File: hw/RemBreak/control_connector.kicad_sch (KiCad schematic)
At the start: 1 part, among them J5 Conn_02x06_Odd_Even

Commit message: routing in progress
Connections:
- net +3V3: now also J5.6 (Pin_6); no longer J5.3 (Pin_3)
- net +5V: now also J5.5 (Pin_5); no longer J5.4 (Pin_4)
- net ON/OFF: now also J5.3 (Pin_3); no longer J5.5 (Pin_5)
- net VBATT: now also J5.4 (Pin_4); no longer J5.6 (Pin_6)
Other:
- moved on the sheet: J5
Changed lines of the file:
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@@
 	(wire
 		(pts
-			(xy 137.16 72.39) (xy 152.4 72.39)
+			(xy 163.83 93.98) (xy 179.07 93.98)
 		)
 		(stroke
@@
 	(wire
 		(pts
-			(xy 137.16 77.47) (xy 152.4 77.47)
+			(xy 163.83 96.52) (xy 179.07 96.52)
 		)
 		(stroke
@@
 	(wire
 		(pts
-			(xy 139.7 66.04) (xy 139.7 74.93)
-		)
-		(stroke
-			(width 0)
-			(type default)
-		)
-	)
-	(wire
-		(pts
-			(xy 121.92 66.04) (xy 121.92 74.93)
-		)
-		(stroke
-			(width 0)
-			(type default)
-		)
-	)
-	(wire
-		(pts
-			(xy 109.22 85.09) (xy 124.46 85.09)
-		)
-		(stroke
-			(width 0)
-			(type default)
-		)
-	)
-	(wire
-		(pts
-			(xy 109.22 77.47) (xy 124.46 77.47)
-		)
-		(stroke
-			(width 0)
-			(type default)
-		)
-	)
-	(wire
-		(pts
-			(xy 121.92 74.93) (xy 124.46 74.93)
-		)
-		(stroke
-			(width 0)
-			(type default)
-		)
-	)
-	(wire
-		(pts
-			(xy 137.16 82.55) (xy 152.4 82.55)
+			(xy 148.59 87.63) (xy 148.59 99.06)
+		)
+		(stroke
+			(width 0)
+			(type default)
+		)
+	)
+	(wire
+		(pts
+			(xy 135.89 106.68) (xy 151.13 106.68)
+		)
+		(stroke
+			(width 0)
+			(type default)
+		)
+	)
+	(wire
+		(pts
+			(xy 135.89 96.52) (xy 151.13 96.52)
+		)
+		(stroke
+			(width 0)
+			(type default)
+		)
+	)
+	(wire
+		(pts
+			(xy 163.83 104.14) (xy 179.07 104.14)
 		)
 		(stroke
@@
 	(wire
 		(pts
-			(xy 139.7 74.93) (xy 137.16 74.93)
-		)
-		(stroke
-			(width 0)
-			(type default)
-		)
-	)
-	(wire
-		(pts
 			(xy 41.91 104.14) (xy 41.91 107.95)
 		)
@@
 	(wire
 		(pts
-			(xy 137.16 80.01) (xy 152.4 80.01)
-		)
-		(stroke
-			(width 0)
-			(type default)
-		)
-	)
-	(wire
-		(pts
-			(xy 109.22 80.01) (xy 124.46 80.01)
-		)
-		(stroke
-			(width 0)
-			(type default)
-		)
-	)
-	(wire
-		(pts
-			(xy 109.22 72.39) (xy 124.46 72.39)
-		)
-		(stroke
-			(width 0)
-			(type default)
-		)
-	)
-	(wire
-		(pts
-			(xy 109.22 82.55) (xy 124.46 82.55)
+			(xy 163.83 101.6) (xy 179.07 101.6)
+		)
+		(stroke
+			(width 0)
+			(type default)
+		)
+	)
+	(wire
+		(pts
+			(xy 135.89 101.6) (xy 151.13 101.6)
+		)
+		(stroke
+			(width 0)
+			(type default)
+		)
+	)
+	(wire
+		(pts
+			(xy 135.89 93.98) (xy 151.13 93.98)
+		)
+		(stroke
+			(width 0)
+			(type default)
+		)
+	)
+	(wire
+		(pts
+			(xy 135.89 104.14) (xy 151.13 104.14)
+		)
+		(stroke
+			(width 0)
+			(type default)
+		)
+	)
+	(wire
+		(pts
+			(xy 166.37 99.06) (xy 163.83 99.06)
+		)
+		(stroke
+			(width 0)
+			(type default)
+		)
+	)
+	(wire
+		(pts
+			(xy 148.59 99.06) (xy 151.13 99.06)
+		)
+		(stroke
+			(width 0)
+			(type default)
+		)
+	)
+	(wire
+		(pts
+			(xy 166.37 87.63) (xy 166.37 99.06)
 		)
 		(stroke
@@
 	(wire
 		(pts
-			(xy 137.16 85.09) (xy 139.7 85.09)
+			(xy 163.83 106.68) (xy 166.37 106.68)
 		)
 		(stroke
@@
 	)
 	(label "VBATT"
-		(at 152.4 77.47 180)
+		(at 179.07 96.52 180)
 		(fields_autoplaced yes)
 		(effects
@@
 	)
 	(label "LED BLUE"
-		(at 152.4 80.01 180)
+		(at 179.07 101.6 180)
 		(fields_autoplaced yes)
 		(effects
@@
 	)
 	(label "ONOFF"
-		(at 109.22 77.47 0)
+		(at 135.89 96.52 0)
 		(fields_autoplaced yes)
 		(effects
@@
 	)
 	(label "DISPLAY.DCKI"
-		(at 109.22 85.09 0)
+		(at 135.89 106.68 0)
 		(fields_autoplaced yes)
 		(effects
@@
 	)
 	(label "DISPLAY.DI"
-		(at 152.4 82.55 180)
+		(at 179.07 104.14 180)
 		(fields_autoplaced yes)
 		(effects
@@
 	)
 	(label "I2C.SCL"
-		(at 109.22 72.39 0)
+		(at 135.89 93.98 0)
 		(fields_autoplaced yes)
 		(effects
@@
 	)
 	(label "I2C.SDA"
-		(at 152.4 72.39 180)
+		(at 179.07 93.98 180)
 		(fields_autoplaced yes)
 		(effects
@@
 	)
 	(label "LED RED"
-		(at 109.22 82.55 0)
+		(at 135.89 104.14 0)
 		(fields_autoplaced yes)
 		(effects
@@
 	)
 	(label "LED GREEN"
-		(at 109.22 80.01 0)
+		(at 135.89 101.6 0)
 		(fields_autoplaced yes)
 		(effects
@@
 	(symbol
 		(lib_id "Connector_Generic:Conn_02x06_Odd_Even")
-		(at 129.54 77.47 0)
+		(at 156.21 99.06 0)
 		(unit 1)
 		(exclude_from_sim no)
@@
 		(dnp no)
 		(property "Reference" "J5"
-			(at 131.064 87.884 0)
+			(at 157.734 109.474 0)
 			(effects
 				(font
@@
 		)
 		(property "Value" "Conn_02x06_Odd_Even"
-			(at 130.81 68.58 0)
+			(at 157.48 90.17 0)
 			(effects
 				(font
@@
 		)
 		(property "Footprint" "chinese_modules:SAMTEC_TSM-106-01-L-DH-P-TR"
-			(at 129.54 77.47 0)
+			(at 156.21 99.06 0)
 			(effects
 				(font
@@
 		)
 		(property "Datasheet" "~"
-			(at 129.54 77.47 0)
+			(at 156.21 99.06 0)
 			(effects
 				(font
@@
 		)
 		(property "Description" "Generic connector, double row, 02x06, odd/even pin numbering scheme (row 1 odd numbers, row 2 even numbers), script generated (kicad-library-utils/schlib/autogen/connector/)"
-			(at 129.54 77.47 0)
+			(at 156.21 99.06 0)
 			(effects
 				(font
@@
 	(symbol
 		(lib_id "power:GND")
-		(at 139.7 85.09 0)
+		(at 166.37 106.68 0)
 		(unit 1)
 		(exclude_from_sim no)
@@
 		(fields_autoplaced yes)
 		(property "Reference" "#PWR019"
-			(at 139.7 91.44 0)
+			(at 166.37 113.03 0)
 			(effects
 				(font
@@
 		)
 		(property "Value" "GND"
-			(at 139.7 90.17 0)
+			(at 166.37 111.76 0)
 			(effects
 				(font
@@
 		)
 		(property "Footprint" ""
-			(at 139.7 85.09 0)
+			(at 166.37 106.68 0)
 			(effects
 				(font
@@
 		)
 		(property "Datasheet" ""
-			(at 139.7 85.09 0)
+			(at 166.37 106.68 0)
 			(effects
 				(font
@@
 		)
 		(property "Description" "Power symbol creates a global label with name \"GND\" , ground"
-			(at 139.7 85.09 0)
+			(at 166.37 106.68 0)
 			(effects
 				(font
@@
 	(symbol
 		(lib_id "power:+5V")
-		(at 139.7 66.04 0)
+		(at 148.59 87.63 0)
 		(unit 1)
 		(exclude_from_sim no)
@@
 		(fields_autoplaced yes)
 		(property "Reference" "#PWR018"
-			(at 139.7 69.85 0)
+			(at 148.59 91.44 0)
 			(effects
 				(font
@@
 		)
 		(property "Value" "+5V"
-			(at 139.7 60.96 0)
+			(at 148.59 82.55 0)
 			(effects
 				(font
@@
 		)
 		(property "Footprint" ""
-			(at 139.7 66.04 0)
+			(at 148.59 87.63 0)
 			(effects
 				(font
@@
 		)
 		(property "Datasheet" ""
-			(at 139.7 66.04 0)
+			(at 148.59 87.63 0)
 			(effects
 				(font
@@
 		)
 		(property "Description" "Power symbol creates a global label with name \"+5V\""
-			(at 139.7 66.04 0)
+			(at 148.59 87.63 0)
 			(effects
 				(font
@@
 	(symbol
 		(lib_id "power:+3V3")
-		(at 121.92 66.04 0)
+		(at 166.37 87.63 0)
 		(unit 1)
 		(exclude_from_sim no)
@@
 		(fields_autoplaced yes)
 		(property "Reference" "#PWR017"
-			(at 121.92 69.85 0)
+			(at 166.37 91.44 0)
 			(effects
 				(font
@@
 		)
 		(property "Value" "+3V3"
-			(at 121.92 60.96 0)
+			(at 166.37 82.55 0)
 			(effects
 				(font
@@
 		)
 		(property "Footprint" ""
-			(at 121.92 66.04 0)
+			(at 166.37 87.63 0)
 			(effects
 				(font
@@
 		)
 		(property "Datasheet" ""
-			(at 121.92 66.04 0)
+			(at 166.37 87.63 0)
 			(effects
 				(font
@@
 		)
 		(property "Description" "Power symbol creates a global label with name \"+3V3\""
-			(at 121.92 66.04 0)
-			(effects
-				(font
+			(at 166.37 87.63 0)
+			(effects
+				(font

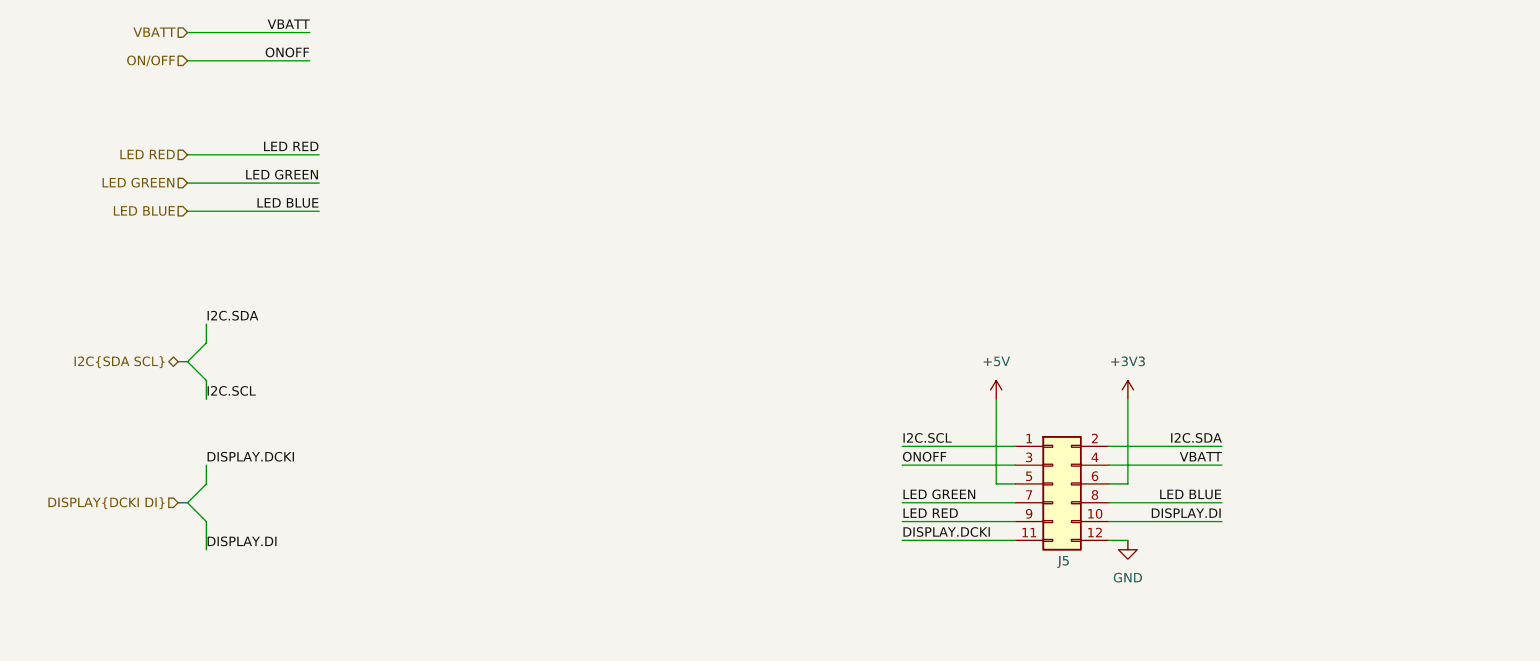
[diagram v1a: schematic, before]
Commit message: first version of routing finished
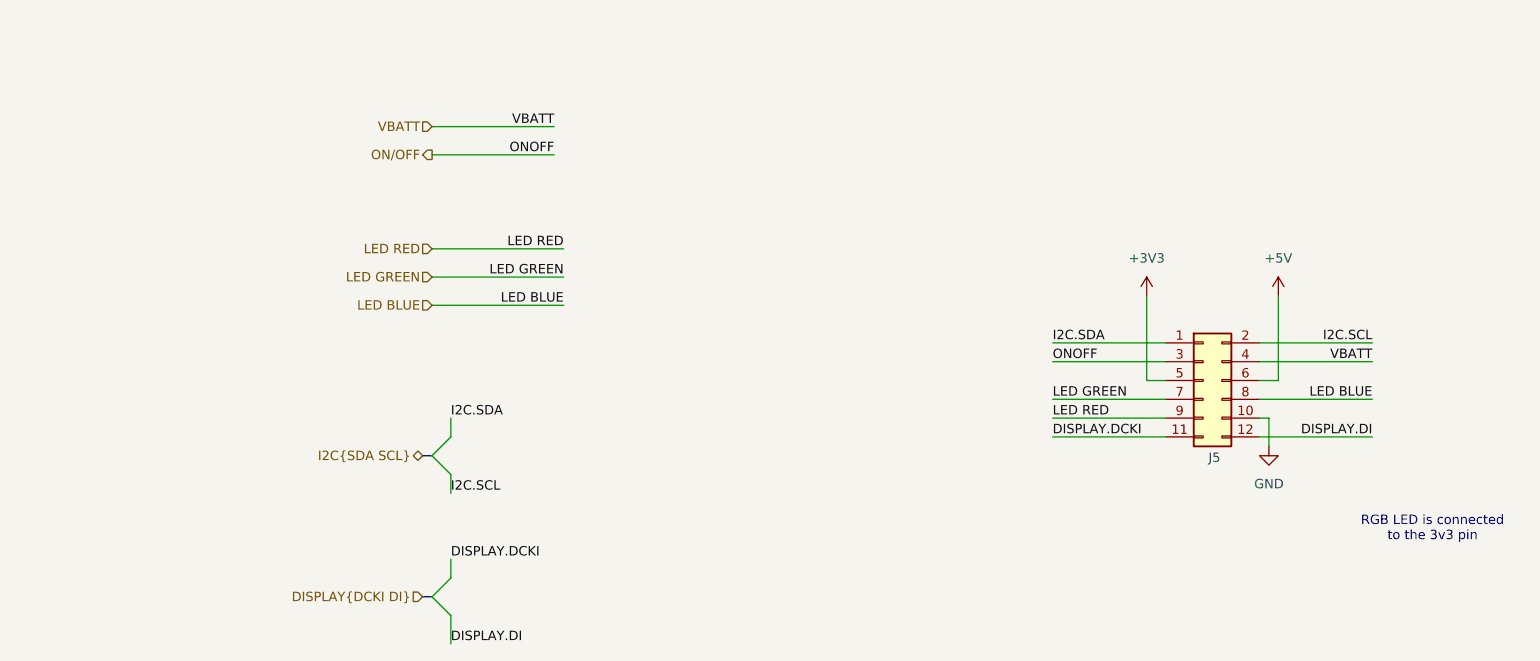
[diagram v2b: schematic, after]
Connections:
- net +3V3: now also J5.5 (Pin_5); no longer J5.6 (Pin_6)
- net +5V: now also J5.6 (Pin_6); no longer J5.5 (Pin_5)
- net DISPLAY.DI: now also J5.12 (Pin_12); no longer J5.10 (Pin_10)
- net GND: now also J5.10 (Pin_10); no longer J5.12 (Pin_12)
- net I2C.SCL: now also J5.2 (Pin_2); no longer J5.1 (Pin_1)
- net I2C.SDA: now also J5.1 (Pin_1); no longer J5.2 (Pin_2)
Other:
- note added: "RGB LED is connected to the 3v3 pin"
- moved on the sheet: J5

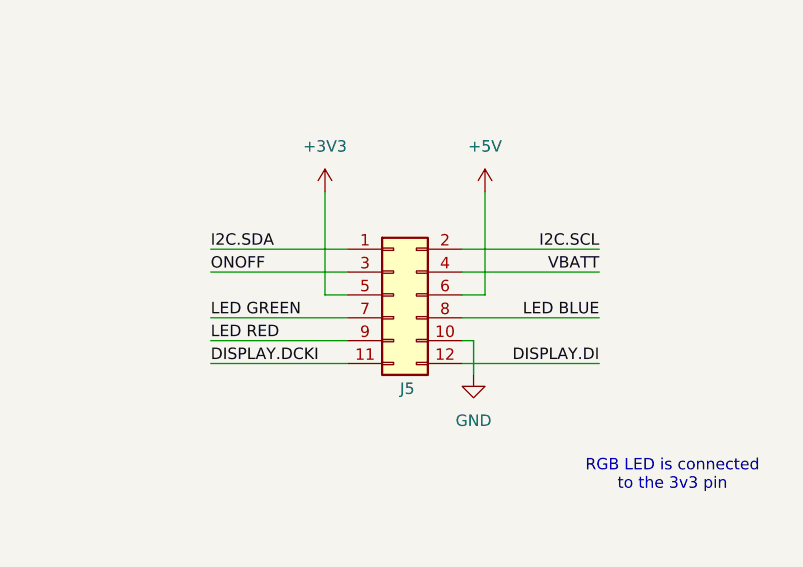
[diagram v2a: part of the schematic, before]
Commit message: partially reorganized components and routing
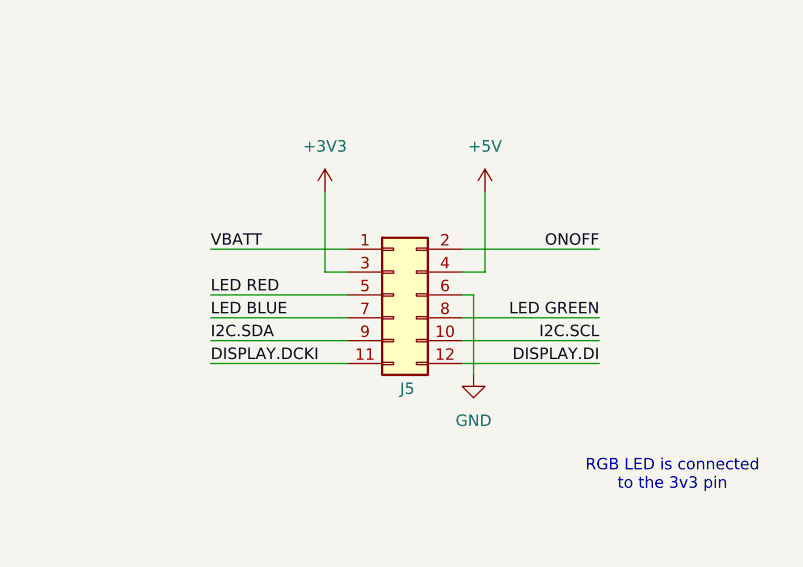
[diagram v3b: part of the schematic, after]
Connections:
- net +3V3: now also J5.3 (Pin_3); no longer J5.5 (Pin_5)
- net +5V: now also J5.4 (Pin_4); no longer J5.6 (Pin_6)
- net GND: now also J5.6 (Pin_6); no longer J5.10 (Pin_10)
- net I2C.SCL: now also J5.10 (Pin_10); no longer J5.2 (Pin_2)
- net I2C.SDA: now also J5.9 (Pin_9); no longer J5.1 (Pin_1)
- net LED BLUE: now also J5.7 (Pin_7); no longer J5.8 (Pin_8)
- net LED GREEN: now also J5.8 (Pin_8); no longer J5.7 (Pin_7)
- net LED RED: now also J5.5 (Pin_5); no longer J5.9 (Pin_9)
- net ON/OFF: now also J5.2 (Pin_2); no longer J5.3 (Pin_3)
- net VBATT: now also J5.1 (Pin_1); no longer J5.4 (Pin_4)
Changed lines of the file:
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@@
+	(wire
+		(pts
+			(xy 184.15 87.63) (xy 199.39 87.63)
+		)
+		(stroke
+			(width 0)
+			(type default)
+		)
+	)
 	(wire
 		(pts
@@
 	(wire
 		(pts
+			(xy 184.15 85.09) (xy 185.42 85.09)
+		)
+		(stroke
+			(width 0)
+			(type default)
+		)
+	)
+	(wire
+		(pts
 			(xy 72.39 50.8) (xy 88.9 50.8)
 		)
@@
 	(wire
 		(pts
-			(xy 184.15 82.55) (xy 199.39 82.55)
+			(xy 156.21 85.09) (xy 171.45 85.09)
 		)
 		(stroke
@@
 	(wire
 		(pts
-			(xy 168.91 73.66) (xy 168.91 85.09)
+			(xy 185.42 85.09) (xy 185.42 93.98)
+		)
+		(stroke
+			(width 0)
+			(type default)
+		)
+	)
+	(wire
+		(pts
+			(xy 168.91 73.66) (xy 168.91 82.55)
 		)
 		(stroke
@@
 	(wire
 		(pts
-			(xy 156.21 82.55) (xy 171.45 82.55)
-		)
-		(stroke
-			(width 0)
-			(type default)
-		)
-	)
-	(wire
-		(pts
-			(xy 185.42 90.17) (xy 185.42 93.98)
+			(xy 156.21 87.63) (xy 171.45 87.63)
+		)
+		(stroke
+			(width 0)
+			(type default)
+		)
+	)
+	(wire
+		(pts
+			(xy 168.91 82.55) (xy 171.45 82.55)
 		)
 		(stroke
@@
 	(wire
 		(pts
-			(xy 184.15 90.17) (xy 185.42 90.17)
+			(xy 184.15 82.55) (xy 186.69 82.55)
 		)
 		(stroke
@@
 	(wire
 		(pts
-			(xy 184.15 87.63) (xy 199.39 87.63)
-		)
-		(stroke
-			(width 0)
-			(type default)
-		)
-	)
-	(wire
-		(pts
-			(xy 156.21 87.63) (xy 171.45 87.63)
+			(xy 184.15 90.17) (xy 199.39 90.17)
 		)
 		(stroke
@@
 	(wire
 		(pts
-			(xy 186.69 85.09) (xy 184.15 85.09)
-		)
-		(stroke
-			(width 0)
-			(type default)
-		)
-	)
-	(wire
-		(pts
-			(xy 168.91 85.09) (xy 171.45 85.09)
-		)
-		(stroke
-			(width 0)
-			(type default)
-		)
-	)
-	(wire
-		(pts
-			(xy 186.69 73.66) (xy 186.69 85.09)
+			(xy 186.69 73.66) (xy 186.69 82.55)
 		)
 		(stroke
@@
 	)
 	(label "VBATT"
-		(at 199.39 82.55 180)
-		(fields_autoplaced yes)
-		(effects
-			(font
-				(size 1.27 1.27)
-			)
-			(justify right bottom)
+		(at 156.21 80.01 0)
+		(fields_autoplaced yes)
+		(effects
+			(font
+				(size 1.27 1.27)
+			)
+			(justify left bottom)
 		)
 	)
@@
 	)
 	(label "LED BLUE"
-		(at 199.39 87.63 180)
-		(fields_autoplaced yes)
-		(effects
-			(font
-				(size 1.27 1.27)
-			)
-			(justify right bottom)
+		(at 156.21 87.63 0)
+		(fields_autoplaced yes)
+		(effects
+			(font
+				(size 1.27 1.27)
+			)
+			(justify left bottom)
 		)
 	)
@@
 	)
 	(label "ONOFF"
-		(at 156.21 82.55 0)
-		(fields_autoplaced yes)
-		(effects
-			(font
-				(size 1.27 1.27)
-			)
-			(justify left bottom)
+		(at 199.39 80.01 180)
+		(fields_autoplaced yes)
+		(effects
+			(font
+				(size 1.27 1.27)
+			)
+			(justify right bottom)
 		)
 	)
@@
 	)
 	(label "I2C.SCL"
-		(at 199.39 80.01 180)
+		(at 199.39 90.17 180)
 		(fields_autoplaced yes)
 		(effects
@@
 	)
 	(label "I2C.SDA"
-		(at 156.21 80.01 0)
+		(at 156.21 90.17 0)
 		(fields_autoplaced yes)
 		(effects
@@
 	)
 	(label "LED RED"
-		(at 156.21 90.17 0)
+		(at 156.21 85.09 0)
 		(fields_autoplaced yes)
 		(effects
@@
 	)
 	(label "LED GREEN"
-		(at 156.21 87.63 0)
-		(fields_autoplaced yes)
-		(effects
-			(font
-				(size 1.27 1.27)
-			)
-			(justify left bottom)
-		)
-	)
+		(at 199.39 87.63 180)
+		(fields_autoplaced yes)
+		(effects
+			(font
+				(size 1.27 1.27)
+			)
+			(justify right bottom)
+		)
+	)

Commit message: components placed and tracks routed - missing gnd connections and have to refactor the resistors under MCU
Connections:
- net DISPLAY.DCKI: now also J5.9 (Pin_9); no longer J5.11 (Pin_11)
- net DISPLAY.DI: now also J5.10 (Pin_10); no longer J5.12 (Pin_12)
- net I2C.SCL: now also J5.12 (Pin_12); no longer J5.10 (Pin_10)
- net I2C.SDA: now also J5.11 (Pin_11); no longer J5.9 (Pin_9)
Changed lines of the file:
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@@
 	)
 	(label "DISPLAY.DCKI"
-		(at 156.21 92.71 0)
+		(at 156.21 90.17 0)
 		(fields_autoplaced yes)
 		(effects
@@
 	)
 	(label "DISPLAY.DI"
-		(at 199.39 92.71 180)
+		(at 199.39 90.17 180)
 		(fields_autoplaced yes)
 		(effects
@@
 	)
 	(label "I2C.SCL"
-		(at 199.39 90.17 180)
+		(at 199.39 92.71 180)
 		(fields_autoplaced yes)
 		(effects
@@
 	)
 	(label "I2C.SDA"
-		(at 156.21 90.17 0)
+		(at 156.21 92.71 0)
 		(fields_autoplaced yes)
 		(effects

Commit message: Note fonts changed to bold and added titles of the sheets included rev number
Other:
- note added: "RGB LED (Common anode) connected to 3V3"
- note removed: "RGB LED is connected to the 3v3 pin"
- title: (none) -> Control Connector
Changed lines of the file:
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@@
 	(generator_version "8.99")
 	(paper "A4")
-	(text "RGB LED is connected\nto the 3v3 pin"
+	(title_block
+		(title "Control Connector")
+		(date "2024-12-15")
+		(rev "1.0")
+	)
+	(text "RGB LED (Common anode)\nconnected to 3V3"
 		(exclude_from_sim no)
-		(at 207.518 105.156 0)
+		(at 179.07 107.188 0)
 		(effects
 			(font
 				(size 1.27 1.27)
+				(thickness 0.254)
+				(bold yes)
 			)
 		)
